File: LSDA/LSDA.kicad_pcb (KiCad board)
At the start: 2 copper layers, 76 parts, among them Q1 BC547, Q2 BC547, U1 LM324

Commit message: Revision 2
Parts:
- removed C2 (x2): 10uF, diy-nabra:cel1
- removed R12 (x2): 100k, diy-nabra:r3
- removed R13 (x2): 10k, diy-nabra:r3
- removed the R7 at (36.9, 126.9)
- removed the REF** at (87.4, 139.7)
- removed the REF** at (74.3, 101.6)
- removed the REF** at (31.8, 139.7)
- removed the REF** at (45.0, 101.6)
- added C4: 1uF, diy-nabra:cpoly105, F.Cu at (68.8, 87.8)
- added C4: 1uF, diy-nabra:cpoly105, B.Cu at (50.5, 87.8)
- added C5: 1uF, diy-nabra:cpoly105, F.Cu at (68.8, 113.4)
- added C5: 1uF, diy-nabra:cpoly105, B.Cu at (50.5, 113.4)
- added R21: 100k, diy-nabra:r3, F.Cu at (71.8, 95.2)
- added R21: 100k, diy-nabra:r3, B.Cu at (47.5, 95.2)
- added R22: 68k, diy-nabra:r3, F.Cu at (63.5, 97.8)
- added R22: 68k, diy-nabra:r3, B.Cu at (55.8, 97.8)
- added R23: 68k, diy-nabra:r3, F.Cu at (71.1, 102.2)
- added R23: 68k, diy-nabra:r3, B.Cu at (48.1, 102.2)
- added R24: 100k, diy-nabra:r3, F.Cu at (64.4, 107.4)
- added R24: 100k, diy-nabra:r3, B.Cu at (54.9, 107.4)
- added R7: 0, diy-nabra:r3, F.Cu at (85.0, 133.2)
- added R7: 10k, diy-nabra:r3, B.Cu at (39.3, 130.2)
- added R7: 0, diy-nabra:r3, B.Cu at (34.2, 133.2)
- added REF**: cpoly105, diy-nabra:cpoly105, F.Cu at (113.7, 109.2)
- RV1 (x2): value B100K -> B25k
- moved REF** 81.9 mm to (113.7, 151.8)
- moved REF** 79.4 mm to (113.7, 66.0)
- moved REF** 35.6 mm to (113.7, 89.5)
- moved REF** 26.1 mm to (113.7, 127.0)
- moved D2 26.1 mm to (62.9, 116.8), turned to 0 degrees
- moved D2 26.1 mm to (56.4, 116.8), turned to 180 degrees
- moved D1 25.1 mm to (62.9, 85.1), turned to 0 degrees
- moved D1 25.1 mm to (56.4, 85.1), turned to 180 degrees
- moved TP2 23.4 mm to (36.7, 77.5)
- moved TP2 23.4 mm to (82.5, 77.5)
- moved R18 18.0 mm to (36.7, 81.9), turned to -90 degrees
- moved R18 18.0 mm to (82.5, 81.9), turned to -90 degrees
- moved Q2 6.46 mm to (41.8, 125.7), turned to 0 degrees
- moved Q2 6.46 mm to (77.5, 125.7), turned to 180 degrees
- moved C1 6.35 mm to (82.5, 116.8), turned to 90 degrees
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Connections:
- R10 pad 1: GND -> MIDO (x2)
- R18 pad 1: Net-(U1C-+) -> Net-(U1C--) (x2)
- RV1 pad 2: Net-(U1C-+) -> Net-(U1C--) (x2)
- U1 pad 1: Net-(U1C-+) -> Net-(U1C--) (x2)
- U1 pad 10: Net-(U1C-+) -> Vref1 (x2)
- U1 pad 13: Net-(U1C-+) -> Vref2 (x2)
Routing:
- net Net-(U1C-+): track 96.5 -> 0.00 mm
- net Net-(U1C--): track 55.8 -> 91.1 mm
- net Vref2: track 0.00 -> 29.4 mm
- net Vref1: track 0.00 -> 29.1 mm
- net Net-(R6-Pad2): track 74.9 -> 101.0 mm
- net GND: track 263.4 -> 238.0 mm
- net +9V: track 432.8 -> 407.9 mm
- net Net-(R3-Pad2): track 63.7 -> 73.0 mm
- net Net-(D1-K): track 11.4 -> 5.39 mm
- net Net-(R20-Pad2): track 17.3 -> 23.0 mm
- net Net-(U1B--): track 15.5 -> 20.4 mm
- net Net-(R11-Pad1): track 22.2 -> 27.1 mm
- net Net-(Q2-C): track 10.0 -> 5.24 mm
- net Net-(R18-Pad2): track 13.3 -> 8.89 mm
- net Net-(U1A--): track 70.5 -> 73.2 mm
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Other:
- board text added: "10uF polarised cap"
- board text added: "1uF MLCC cap"
- board text added: "B25k"
- board text added: "BC547/8/9"
- board text added: "Neil Massey 2025 (v2)"
- board text removed: "100uF polcap"
- board text removed: "B100k"
- board text removed: "BC547"
- board text removed: "Neil Massey 2025"

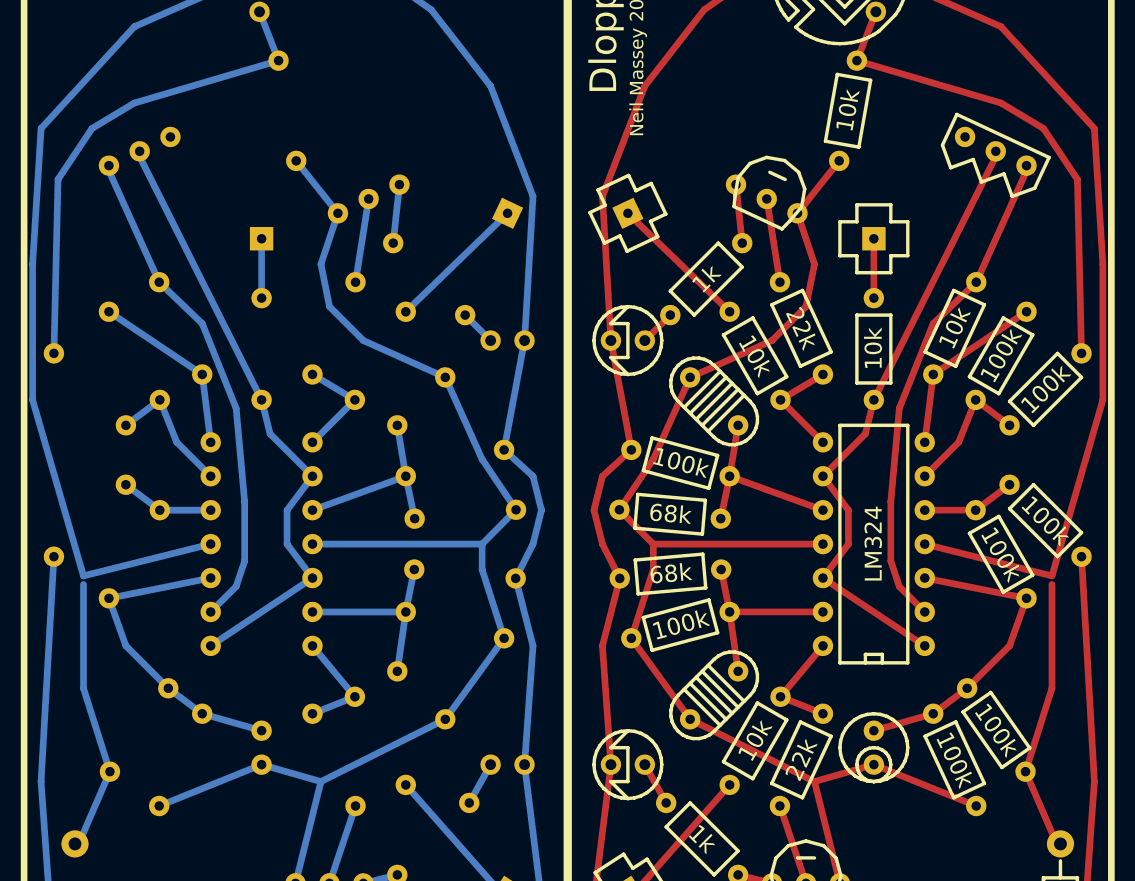
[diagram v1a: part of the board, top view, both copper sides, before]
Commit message: Fixed broken track
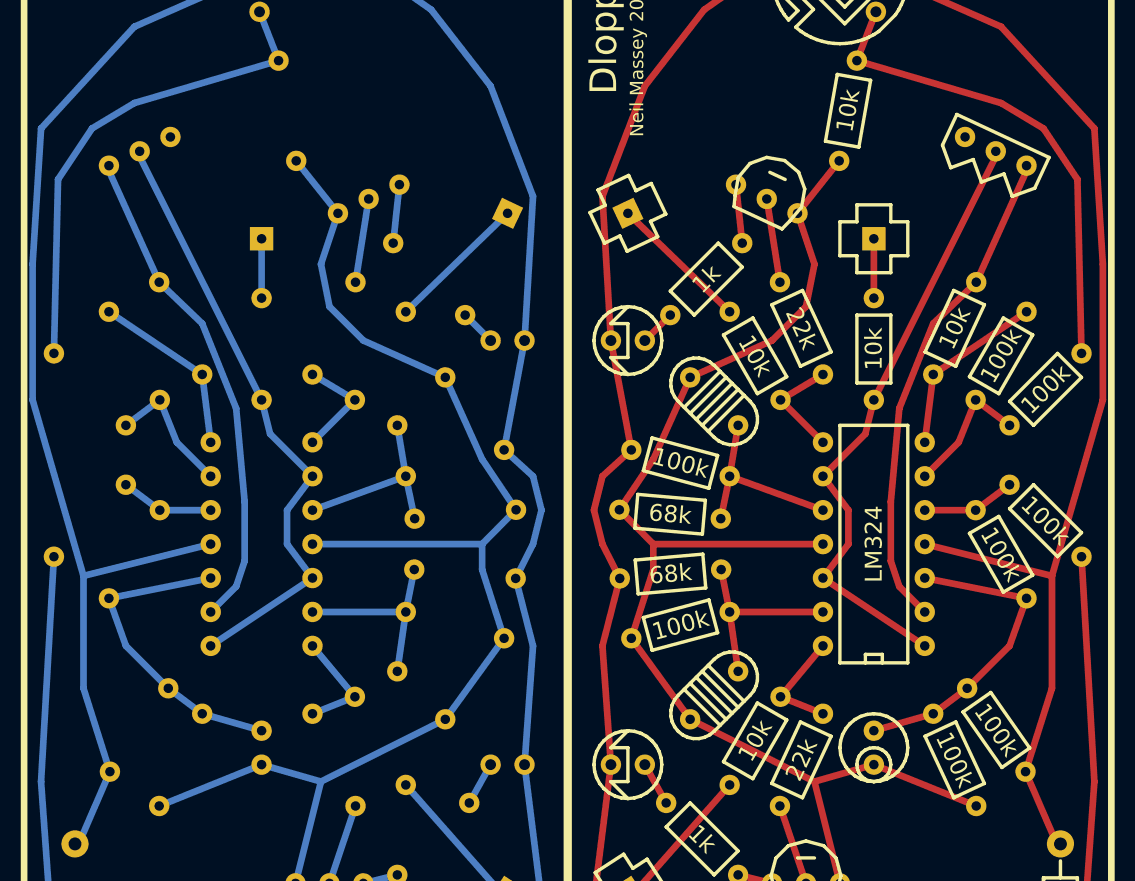
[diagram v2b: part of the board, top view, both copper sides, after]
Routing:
- net +9V: track 407.9 -> 409.2 mm
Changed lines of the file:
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@@
 		)
 		(property "Value" "100k"
-			(at 3.81 0.000002 115)
+			(at 3.810001 0.000002 115)
 			(layer "F.SilkS")
 			(effects
@@
 		(tags "qnpn from Ciat-Lonbarde Osmond PCB library")
 		(property "Reference" "Q2"
-			(at 0.000001 4.445 360)
+			(at 0.000001 4.445 0)
 			(layer "F.Fab")
 			(effects
@@
 		)
 		(property "Value" "BC547"
-			(at 0 -3.175 360)
+			(at 0 -3.175 0)
 			(layer "F.SilkS")
 			(hide yes)
@@
 		)
 		(property "Footprint" "diy-nabra:qnpn"
-			(at 0 0 360)
+			(at 0 0 0)
 			(layer "F.Fab")
 			(hide yes)
@@
 		)
 		(property "Datasheet" "https://www.onsemi.com/pub/Collateral/BC550-D.pdf"
-			(at 0 0 360)
+			(at 0 0 0)
 			(layer "F.Fab")
 			(hide yes)
@@
 		)
 		(property "Description" "0.1A Ic, 45V Vce, Small Signal NPN Transistor, TO-92"
-			(at 0 0 360)
+			(at 0 0 0)
 			(layer "F.Fab")
 			(hide yes)
@@
 		(tags "led from Ciat-Lonbarde Osmond PCB library")
 		(property "Reference" "D1"
-			(at 1.269999 3.81 360)
+			(at 1.269999 3.81 0)
 			(layer "F.Fab")
 			(effects
@@
 		)
 		(property "Value" "LED"
-			(at 1.269999 -3.81 360)
+			(at 1.269999 -3.81 0)
 			(layer "F.SilkS")
 			(hide yes)
@@
 		)
 		(property "Footprint" "diy-nabra:led"
-			(at 0 0 360)
+			(at 0 0 0)
 			(layer "F.Fab")
 			(hide yes)
@@
 		)
 		(property "Datasheet" ""
-			(at 0 0 360)
+			(at 0 0 0)
 			(layer "F.Fab")
 			(hide yes)
@@
 		)
 		(property "Description" "Light emitting diode"
-			(at 0 0 360)
+			(at 0 0 0)
 			(layer "F.Fab")
 			(hide yes)
@@
 		)
 		(property "Value" "10k"
-			(at 3.810002 0 80)
+			(at 3.810003 0 80)
 			(layer "F.SilkS")
 			(effects
@@
 		)
 		(pad "1" thru_hole circle
-			(at 7.62 0 290)
+			(at 7.62 0.000001 290)
 			(size 1.524 1.524)
 			(drill 0.7112)
@@
 		(fp_line
 			(start 1.981201 -1.549401)
-			(end 2.2606 -0.762)
+			(end 2.260599 -0.762)
 			(stroke
 				(width 0.254)
@@
 		)
 		(fp_line
-			(start 2.2606 -0.762)
+			(start 2.260599 -0.762)
 			(end 2.616201 0.5588)
 			(stroke
@@
 	)
 	(segment
-		(start 95.885 103.34625)
-		(end 95.885 111.125)
-		(width 0.5)
-		(layer "F.Cu")
-		(net 5)
-	)
-	(segment
 		(start 66.04 138.43)
 		(end 61.595 127)
@@
 	)
 	(segment
-		(start 95.885 111.125)
-		(end 93.905652 117.366938)
+		(start 62.23 107.95)
+		(end 63.528996 102.899127)
 		(width 0.5)
 		(layer "F.Cu")
@@
 	)
 	(segment
-		(start 62.23 107.95)
-		(end 63.528996 102.899127)
+		(start 95.885 111.125)
+		(end 93.905652 117.366938)
 		(width 0.5)
 		(layer "F.Cu")
@@
 	)
 	(segment
+		(start 95.885 102.71125)
+		(end 95.885 111.125)
+		(width 0.5)
+		(layer "F.Cu")
+		(net 5)
+	)
+	(segment
 		(start 63.528996 102.899127)
 		(end 62.23 100.33)
@@
 	)
 	(segment
+		(start 23.378308 102.71125)
+		(end 23.378308 111.125)
+		(width 0.5)
+		(layer "B.Cu")
+		(net 5)
+	)
+	(segment
 		(start 41.947385 146.839077)
 		(end 53.223308 138.43)
@@
 	)
 	(segment
-		(start 23.378308 111.125)
-		(end 25.357656 117.366938)
-		(width 0.5)
-		(layer "B.Cu")
-		(net 5)
-	)
-	(segment
 		(start 57.033308 107.95)
 		(end 55.734312 102.899127)
@@
 	)
 	(segment
-		(start 23.378308 103.34625)
-		(end 23.378308 111.125)
+		(start 23.378308 111.125)
+		(end 25.357656 117.366938)
 		(width 0.5)
 		(layer "B.Cu")
